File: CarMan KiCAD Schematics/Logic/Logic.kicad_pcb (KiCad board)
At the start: 2 copper layers, 57.8 x 76.4 mm, 65 parts, among them J1 J1 MC Can Line, J2 J2 NI I2C, J3 J3 Logic-TSI, J4 J4 GLV BOB, J5 J5 PICKit 3, J6 J6 NI CAN, U1 MCP9700AT-HTT-Sensor_Temperat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, U10 BNO_055, U11 Raspberry_Pi_RTC, U2 ISO1050DUB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

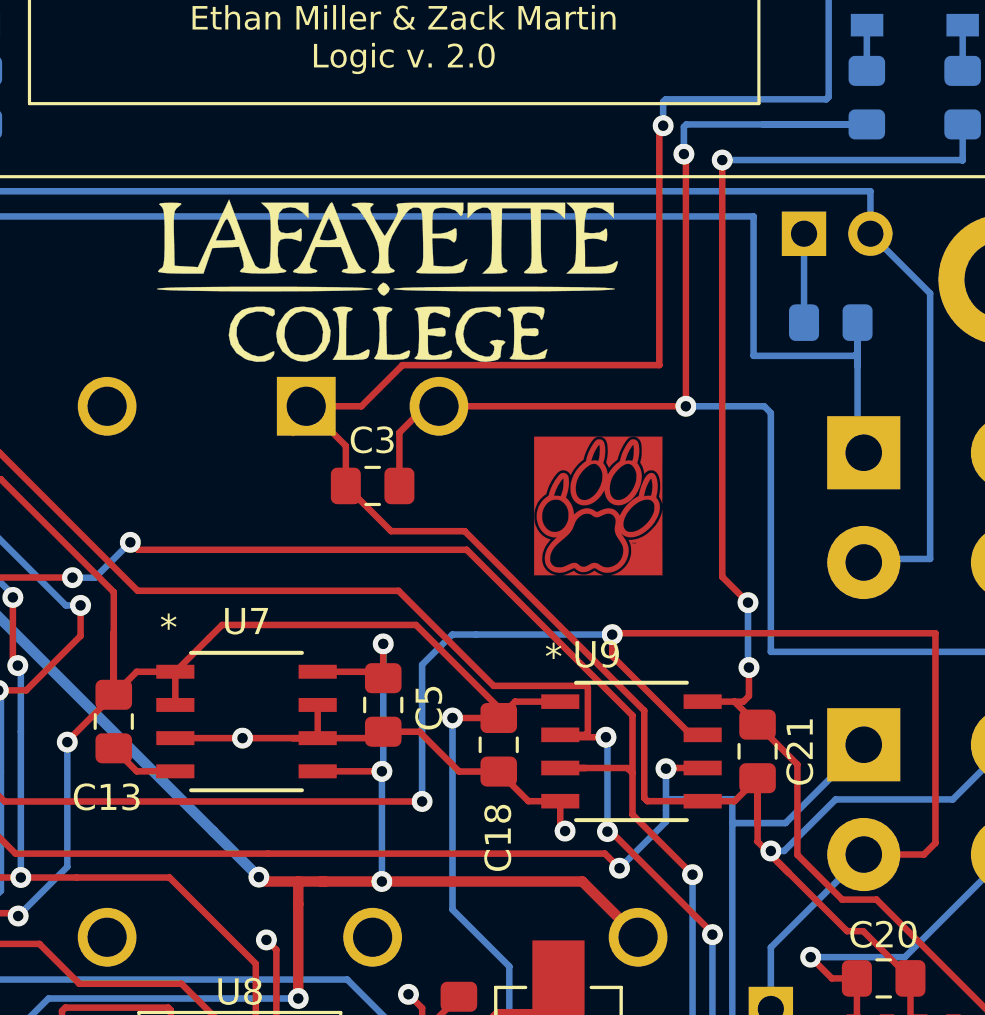
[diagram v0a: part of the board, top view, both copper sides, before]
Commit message: LOGIC: Added pull-up resistors on non-isolated side of I2C TSI:   Added silkscreen labeling and comments GLV:   Organized GLV schematic, increased mounting hole size to 3.5mm from 2.5mm
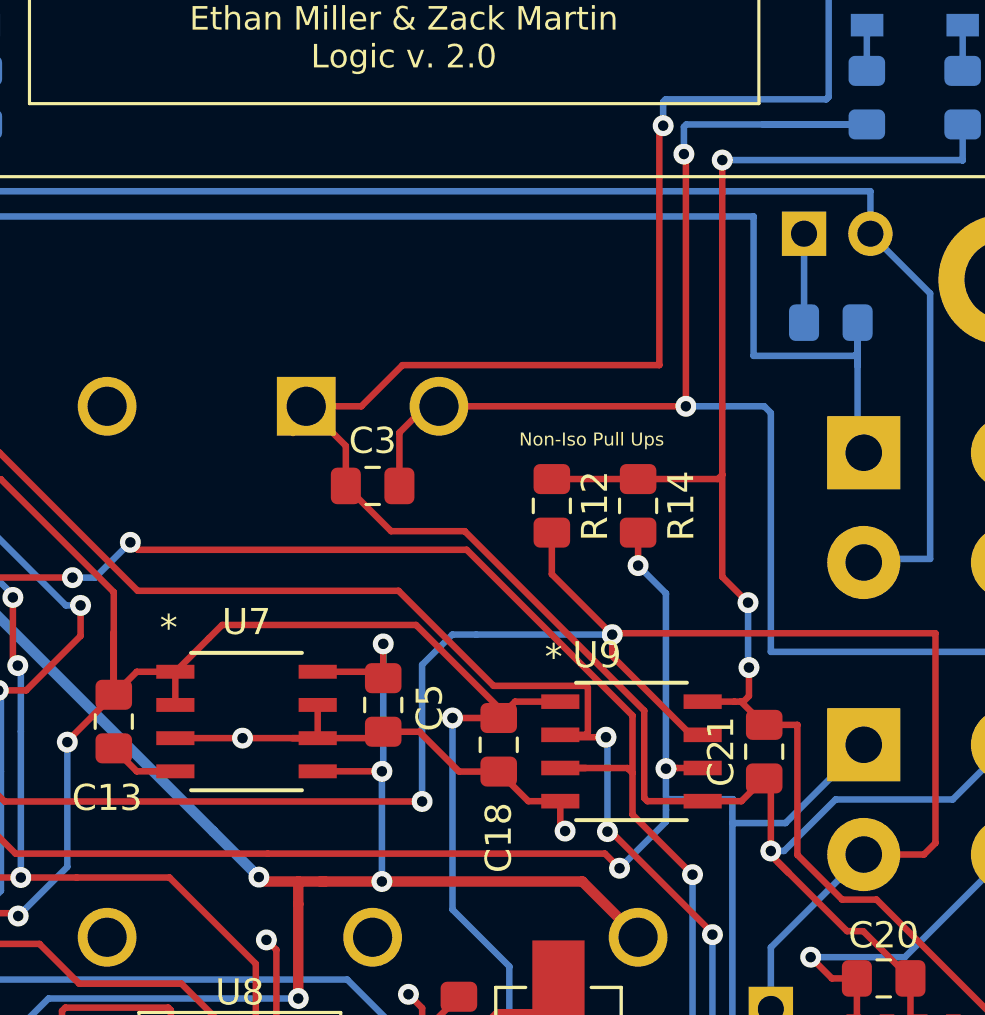
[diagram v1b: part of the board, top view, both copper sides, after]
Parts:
- removed G***: LOGO, CarMan General Footprints:Laf_College_Logo
- removed VAL: REF, CarMan General Footprints:lafLogo
- added R12: 10k, Resistor_SMD:R_0805_2012Metric_Pad1.15x1.40mm_HandSolder, F.Cu at (206.5, 62.0)
- added R14: 10k, Resistor_SMD:R_0805_2012Metric_Pad1.15x1.40mm_HandSolder, F.Cu at (209.8, 62.0)
- R16: value 10k -> 2K
- R5, R6: value 10k -> 1K
- moved C21 0.25 mm to (214.6, 71.4), turned to 90 degrees
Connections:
- C21 pad 1: /5V_NON_ISO -> /GLV_RTN
- C21 pad 2: /GLV_RTN -> /5V_NON_ISO
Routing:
- net /SCL_TSI_GLV: track 52.6 -> 62.1 mm, vias 2 -> 3
- net /5V_NON_ISO: track 123.8 -> 131.1 mm
- net /SDA_TSI_GLV: track 68.4 -> 73.2 mm
- net /GLV_RTN: track 148.5 -> 146.8 mm
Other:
- board text added: "Non-Iso Pull Ups"

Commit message: labeling?
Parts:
- added G***: LOGO, CarMan General Footprints:Laf_College_Logo, F.Cu at (201.2, 50.5)
- added VAL: REF, CarMan General Footprints:lafLogo, F.Cu at (189.7, 50.0)

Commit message: Updated the logic board schematic and layout
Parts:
- removed G***: LOGO, CarMan General Footprints:Laf_College_Logo
- removed VAL: REF, CarMan General Footprints:lafLogo
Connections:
- J2 pad 1: /SDA_TSI_GLV -> /5V_NON_ISO
- J2 pad 2: /SCL_TSI_GLV -> /GLV_RTN
- J2 pad 3: /5V_NON_ISO -> /SDA_TSI_GLV
- J2 pad 4: /GLV_RTN -> /SCL_TSI_GLV
- J5 pad 4: /PGEC -> /PGED
- J5 pad 5: /PGED -> /PGEC
- R1 pad 1: /SDA_ISO_PI -> /SCL_ISO_PI
- R2 pad 1: /SCL_ISO_PI -> /SDA_ISO_PI
- U3 pad 5: /SCL_ISO_PI -> /SDA_ISO_PI
- U3 pad 6: /SDA_ISO_PI -> /SCL_ISO_PI
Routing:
- net /ISO_RTN: track 155.9 -> 184.6 mm, vias 12 -> 16
- net /5V_NON_ISO: track 131.1 -> 156.4 mm, vias 7 -> 10
- net /SCL_TSI_GLV: track 62.1 -> 74.9 mm, vias 3 -> 4
- net /SDA_ISO_PI: track 164.6 -> 174.5 mm
- net /SDA_TSI_GLV: track 73.2 -> 80.5 mm, vias 2 -> 3
- net /GLV_RTN: track 146.8 -> 151.1 mm, vias 5 -> 4
- net /PGEC: track 20.9 -> 23.2 mm
- net /PGED: track 22.4 -> 23.2 mm, vias 0 -> 3
- net /SCL_ISO_PI: track 146.7 -> 146.9 mm, vias 6 -> 7
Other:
- net class Default: clearance 0.2 -> 0.1778
- rule trace_clearance: 0.2 -> 0.1778
- board text added: "Electrical & Computer Engineering Tafita Rakoto & Marwa Saleh Logic v. 3.0"
- board text removed: "Electrical & Computer Engineering Ethan Miller & Zack Martin Logic v. 2.0"
